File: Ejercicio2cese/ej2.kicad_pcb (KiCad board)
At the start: 4 copper layers, 40.6 x 61 mm, 17 parts, among them J1 DB9-F, J2 CAN, U1 SP3232ECN, U2 AMIS42665TJAA1RG

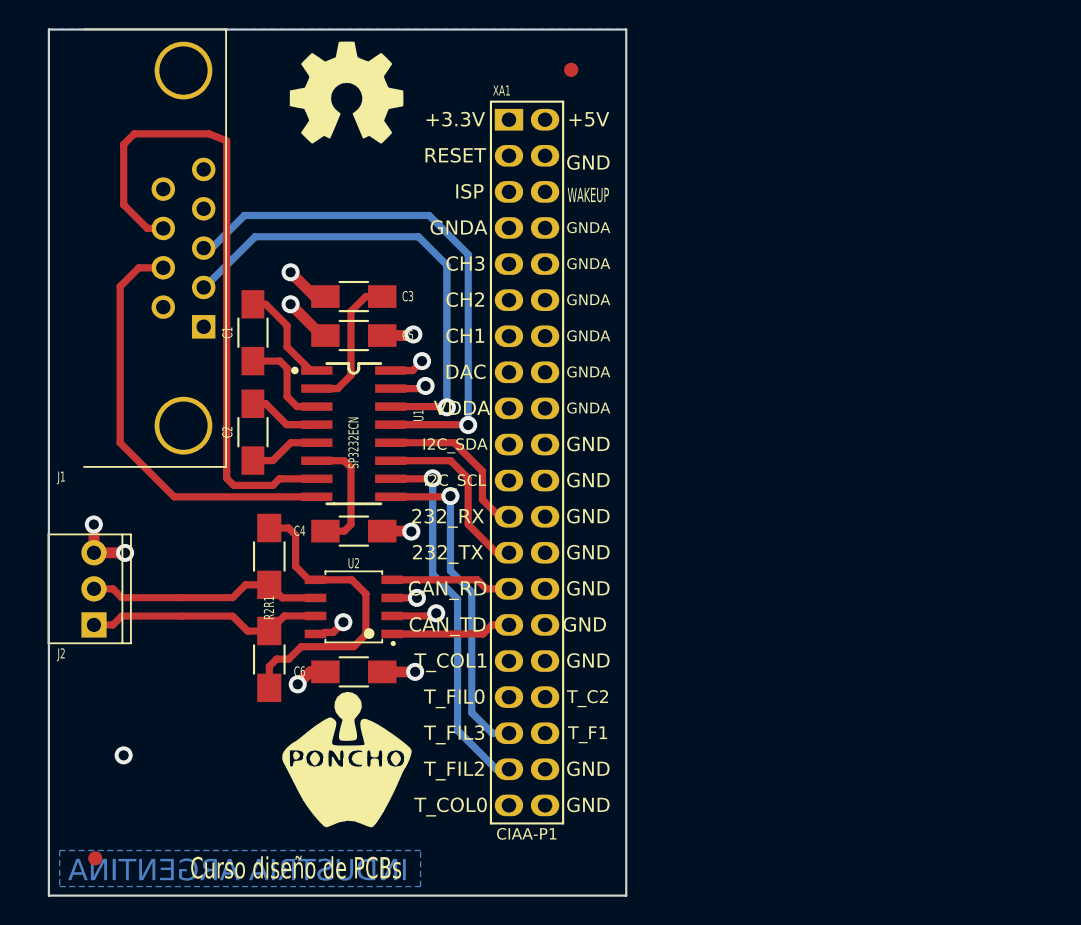
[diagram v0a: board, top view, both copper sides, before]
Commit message: Agrego stackup al Ejercicio2cese.
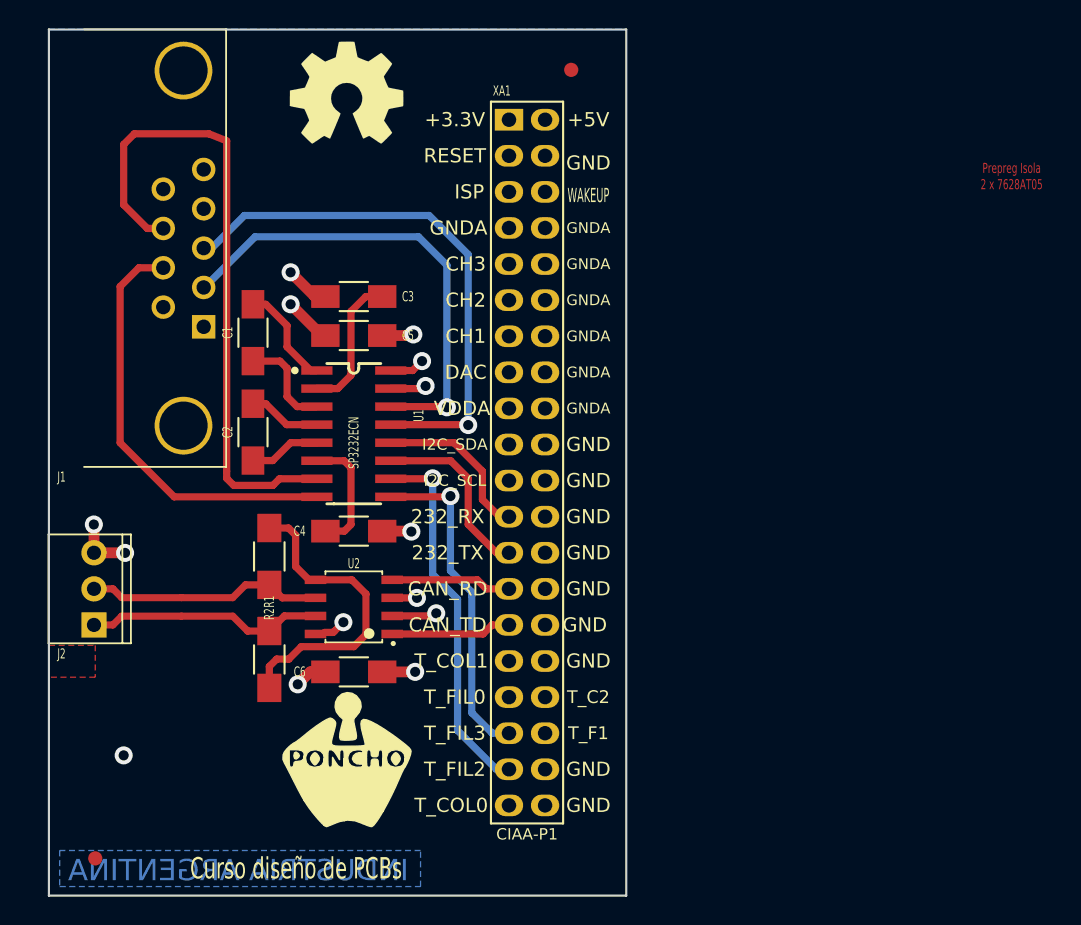
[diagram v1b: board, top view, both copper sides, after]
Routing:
- added copper zone on F.Cu, net (none)
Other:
- board text added: "0,346 mm"
- board text added: "0,760 mm"
- board text added: "1 Oz"
- board text added: "1 Oz = 35 um = 0,035 mm"
- board text added: "L1 - TOP (Signal)"
- board text added: "L2 - GND (Plane)"
- board text added: "L3 - POWER (2 Plane)"
- board text added: "L4 - BOT (Signal)"
- board text added: "Laminate Isola 4 x 7628M"
- board text added: "Prepeg Isola 2 x 7628AT05"
- board text added: "Prepreg Isola 2 x 7628AT05"
- board text removed: "L1 L2"
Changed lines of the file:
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@@
-(kicad_pcb (version 4) (host pcbnew "(2015-09-12 BZR 6188)-product")
+(kicad_pcb (version 4) (host pcbnew 4.0.2+dfsg1-2~bpo8+1-stable)
   (general
     (links 44)
     (no_connects 0)
-    (area 102.159999 73.584999 142.950001 134.695001)
+    (area 80.986905 62.36 236.857859 164.528501)
     (thickness 1.6)
-    (drawings 35)
+    (drawings 52)
     (tracks 169)
     (zones 0)
@@
   (title_block
     (title "Ejercicio 2 - Diseño de PCBs CESE - Poncho RS232 y CAN")
-    (date 2015-11-26)
+    (date 2016-06-03)
     (rev 1.0)
     (company "Instituto Nacional de Tecnología Industrial")
-    (comment 1 "Autores: D.Brengi, D. Alamon y N. Scotti    Licencia:doc/LICENCIA.txt")
+    (comment 1 "Autores: D.Brengi   Licencia:doc/LICENCIA.txt")
   )
   (layers
     (0 TOP signal hide)
     (1 GND power hide)
-    (2 POWER power hide)
-    (31 BOT mixed hide)
+    (2 POWER power)
+    (31 BOT mixed)
     (32 B.Adhes user)
     (33 F.Adhes user hide)
@@
   )
   (setup
-    (last_trace_width 0.508)
+    (last_trace_width 0.3048)
     (user_trace_width 0.3048)
     (user_trace_width 0.4826)
@@
     (user_trace_width 1.27)
     (trace_clearance 0.2794)
-    (zone_clearance 0.3048)
-    (zone_45_only no)
+    (zone_clearance 0.5)
+    (zone_45_only yes)
     (trace_min 0.2794)
     (segment_width 0.127)
@@
       (solder_mask_margin 1.5))
   )
+  (gr_text "1 Oz = 35 um = 0,035 mm" (at 267 109) (layer Dwgs.User)
+    (effects (font (size 1 1) (thickness 0.2)))
+  )
+  (gr_text "0,346 mm" (at 203 97) (layer Dwgs.User)
+    (effects (font (size 1.5 1.5) (thickness 0.2)))
+  )
+  (gr_text "0,760 mm" (at 203 88) (layer Dwgs.User)
+    (effects (font (size 1.5 1.5) (thickness 0.2)))
+  )
+  (gr_text "0,346 mm" (at 203 78) (layer Dwgs.User)
+    (effects (font (size 1.5 1.5) (thickness 0.2)))
+  )
+  (gr_text "1 Oz" (at 199 100) (layer Dwgs.User)
+    (effects (font (size 1 1) (thickness 0.2)))
+  )
+  (gr_text "1 Oz" (at 199 94) (layer Dwgs.User)
+    (effects (font (size 1 1) (thickness 0.2)))
+  )
+  (gr_text "1 Oz" (at 199 81) (layer Dwgs.User)
+    (effects (font (size 1 1) (thickness 0.2)))
+  )
+  (gr_text "1 Oz" (at 199 75) (layer Dwgs.User)
+    (effects (font (size 1 1) (thickness 0.2)))
+  )
+  (gr_text "Laminate Isola\n4 x 7628M" (at 218 87) (layer Dwgs.User)
+    (effects (font (size 1.5 1.5) (thickness 0.2)))
+  )
+  (gr_text "Prepeg Isola\n2 x 7628AT05" (at 218 97) (layer Dwgs.User)
+    (effects (font (size 1.5 1.5) (thickness 0.2)))
+  )
+  (gr_text "Prepeg Isola\n2 x 7628AT05" (at 218 78) (layer Dwgs.User)
+    (effects (font (size 1.5 1.5) (thickness 0.2)))
+  )
+  (gr_text "Prepreg Isola\n2 x 7628AT05" (at 170 84) (layer TOP)
+    (effects (font (size 0.7112 0.4572) (thickness 0.1143)))
+  )
+  (gr_text "L2 - GND (Plane)" (at 242 81) (layer Dwgs.User)
+    (effects (font (size 2 2) (thickness 0.3)))
+  )
+  (gr_text "L4 - BOT (Signal)" (at 229 100) (layer Dwgs.User)
+    (effects (font (size 2 2) (thickness 0.3)) (justify left))
+  )
+  (gr_text "L3 - POWER (2 Plane)" (at 246 94) (layer Dwgs.User)
+    (effects (font (size 2 2) (thickness 0.3)))
+  )
+  (gr_line (start 226.5 100) (end 202 100) (angle 90) (layer Dwgs.User) (width 0.3))
+  (gr_line (start 202 94) (end 226.5 94) (angle 90) (layer Dwgs.User) (width 0.3))
+  (gr_line (start 202.325 81.005) (end 226.455 81.005) (angle 90) (layer Dwgs.User) (width 0.3))
   (gr_text "Colocar \nVerificador\nde layers" (at 87.5 119.9) (layer Dwgs.User)
     (effects (font (size 0.8 0.8) (thickness 0.15)) (justify right))
@@
   (gr_line (start 222.885 164.465) (end 224.79 162.56) (angle 90) (layer Dwgs.User) (width 0.127))
   (gr_line (start 222.885 164.465) (end 220.98 162.56) (angle 90) (layer Dwgs.User) (width 0.127))
-  (gr_text "En un circuito multicapa \nanotar la información del\nstack-up dentro del diseño" (at 170.815 67.31) (layer Dwgs.User)
+  (gr_text "En un circuito multicapa \nanotar la información del\nstack-up dentro del diseño" (at 198 55) (layer Dwgs.User)
     (effects (font (size 2 2) (thickness 0.3) italic) (justify left))
   )
-  (gr_text "L1\n\nL2" (at 203.2 87.63) (layer Dwgs.User)
+  (gr_text "L1 - TOP (Signal)" (at 242 75) (layer Dwgs.User)
     (effects (font (size 2 2) (thickness 0.3)))
   )
-  (gr_line (start 174.625 90.805) (end 198.755 90.805) (angle 90) (layer Dwgs.User) (width 0.3))
-  (gr_line (start 174.625 85.09) (end 198.755 85.09) (angle 90) (layer Dwgs.User) (width 0.3))
-  (gr_text "Terminación superficial: HASL\nEspesor final aprox.: 1,6 mm" (at 191.77 100.965) (layer Dwgs.User)
+  (gr_line (start 202.425 75.005) (end 226.555 75.005) (angle 90) (layer Dwgs.User) (width 0.3))
+  (gr_text "Terminación superficial: HASL\nEspesor final aprox.: 1,6 mm" (at 224 108) (layer Dwgs.User)
     (effects (font (size 2 2) (thickness 0.3)))
   )
-  (gr_text Stack-Up (at 188.595 75.565) (layer Dwgs.User)
+  (gr_text Stack-Up (at 216 64) (layer Dwgs.User)
     (effects (font (size 3 3) (thickness 0.5)))
   )
@@
     )
   )
+  (zone (net 2) (net_name +3.3V) (layer POWER) (hatch edge 0.508)
+    (priority 1)
+    (connect_pads (clearance 0.5))
+    (min_thickness 0.1524)
+    (fill yes (arc_segments 16) (thermal_gap 0.508) (thermal_bridge_width 0.508))
+    (polygon
+      (pts
+        (xy 135.8 74.6) (xy 135.8 110.2) (xy 119.6 110.2) (xy 119.6 107.8) (xy 117.4 105.8)
+        (xy 102.2 105.8) (xy 102.3 74.6)
+      )
+    )
+  )
+  (zone (net 13) (net_name +5V) (layer POWER) (hatch edge 0.508)
+    (connect_pads (clearance 0.2))
+    (min_thickness 0.1524)
+    (fill yes (arc_segments 16) (thermal_gap 0.508) (thermal_bridge_width 0.508))
+    (polygon
+      (pts
+        (xy 141.4 74.6) (xy 102.3 74.6) (xy 102.2 132) (xy 141.4 132)
+      )
+    )
+  )
+  (zone (net 0) (net_name "") (layer TOP) (hatch edge 0.508)
+    (connect_pads (clearance 0))
+    (min_thickness 0.254)
+    (fill yes (arc_segments 16) (thermal_gap 0.508) (thermal_bridge_width 0.762))
+    (polygon
+      (pts
+        (xy 102.25 117) (xy 105.5 117) (xy 105.5 119.25) (xy 102.25 119.25)
+      )
+    )
+  )
   (zone (net 1) (net_name GND) (layer GND) (hatch edge 0.508)
     (connect_pads (clearance 0.2032))
@@
     )
   )
-  (zone (net 2) (net_name +3.3V) (layer POWER) (hatch edge 0.508)
-    (priority 1)
-    (connect_pads (clearance 0.2032))
-    (min_thickness 0.1524)
-    (fill yes (arc_segments 16) (thermal_gap 0.508) (thermal_bridge_width 0.508))
+  (zone (net 0) (net_name "") (layer GND) (hatch edge 0.508)
+    (connect_pads (clearance 0))
+    (min_thickness 0.254)
+    (keepout (tracks allowed) (vias not_allowed) (copperpour not_allowed))
+    (fill (arc_segments 16) (thermal_gap 0.508) (thermal_bridge_width 0.762))
     (polygon
       (pts
-        (xy 135.8 74.6) (xy 135.8 110.2) (xy 119.6 110.2) (xy 119.6 107.8) (xy 117.4 105.8)
-        (xy 103.6 105.8) (xy 103.6 74.6)
+        (xy 102.25 120.75) (xy 105.5 120.75) (xy 105.5 125.75) (xy 102.25 125.75)
       )
     )
   )
-  (zone (net 13) (net_name +5V) (layer POWER) (hatch edge 0.508)
+  (zone (net 0) (net_name "") (layer POWER) (hatch edge 0.508)
     (connect_pads (clearance 0.5))
     (min_thickness 0.1524)
-    (fill yes (arc_segments 16) (thermal_gap 0.508) (thermal_bridge_width 0.508))
+    (keepout (tracks allowed) (vias allowed) (copperpour not_allowed))
+    (fill (arc_segments 16) (thermal_gap 0.508) (thermal_bridge_width 0.508))
     (polygon
       (pts
-        (xy 141.4 74.6) (xy 103.6 74.6) (xy 103.6 132) (xy 141.4 132)
+        (xy 102.25 122.75) (xy 105.5 122.75) (xy 105.5 125.75) (xy 102.25 125.75)
       )
     )

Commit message: Detalles del verificador de capas y limpio bibliotecas del esquemático.
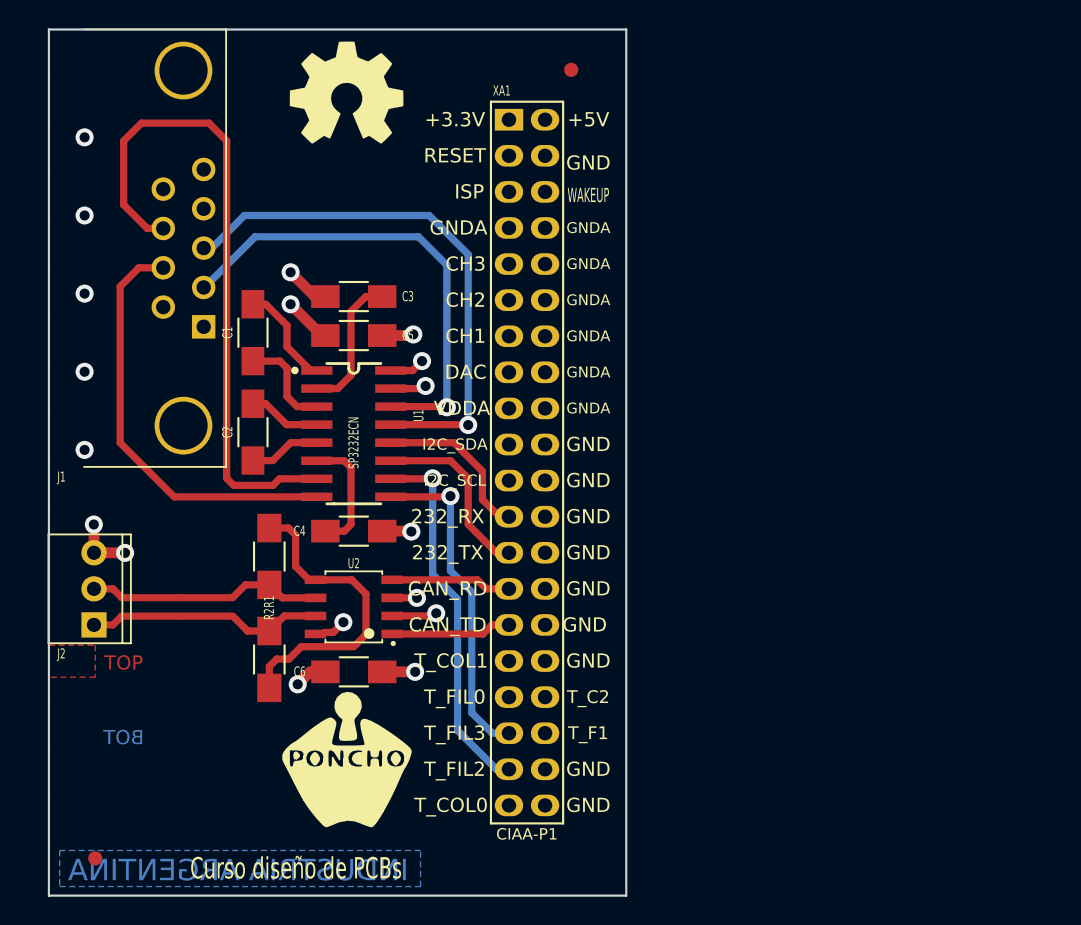
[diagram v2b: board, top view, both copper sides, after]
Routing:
- net GND: track 22.4 -> 52.7 mm, vias 9 -> 14
- net Net-(J1-Pad8): track 45.9 -> 46.8 mm
- net (no net): vias 1 -> 0
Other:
- board text added: "BOT"
- board text added: "GND"
- board text added: "POWER"
- board text added: "TOP"
- board text removed: "Prepreg Isola 2 x 7628AT05"
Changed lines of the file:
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@@
-(kicad_pcb (version 4) (host pcbnew 4.0.2+dfsg1-2~bpo8+1-stable)
+(kicad_pcb (version 4) (host pcbnew "(2015-09-12 BZR 6188)-product")
   (general
     (links 44)
     (no_connects 0)
-    (area 80.986905 62.36 236.857859 164.528501)
+    (area 102.159999 73.584999 142.950001 134.695001)
     (thickness 1.6)
-    (drawings 52)
-    (tracks 169)
+    (drawings 55)
+    (tracks 181)
     (zones 0)
     (modules 17)
@@
   )
   (layers
-    (0 TOP signal hide)
+    (0 TOP signal)
     (1 GND power hide)
-    (2 POWER power)
-    (31 BOT mixed)
+    (2 POWER power hide)
+    (31 BOT signal)
     (32 B.Adhes user)
-    (33 F.Adhes user hide)
+    (33 F.Adhes user)
     (34 B.Paste user)
     (35 F.Paste user)
@@
   )
   (setup
-    (last_trace_width 0.3048)
+    (last_trace_width 0.508)
     (user_trace_width 0.3048)
     (user_trace_width 0.4826)
@@
       (solder_mask_margin 1.5))
   )
+  (gr_text BOT (at 107.5 123.5) (layer BOT)
+    (effects (font (size 1 1) (thickness 0.1)) (justify mirror))
+  )
+  (gr_text POWER (at 108.5 121.75) (layer POWER)
+    (effects (font (size 1 1) (thickness 0.1)))
+  )
+  (gr_text GND (at 107.5 120) (layer GND)
+    (effects (font (size 1 1) (thickness 0.2)))
+  )
+  (gr_text TOP (at 107.5 118.25) (layer TOP)
+    (effects (font (size 1 1) (thickness 0.2)))
+  )
   (gr_text "1 Oz = 35 um = 0,035 mm" (at 267 109) (layer Dwgs.User)
     (effects (font (size 1 1) (thickness 0.2)))
@@
   (gr_text "Prepeg Isola\n2 x 7628AT05" (at 218 78) (layer Dwgs.User)
     (effects (font (size 1.5 1.5) (thickness 0.2)))
-  )
-  (gr_text "Prepreg Isola\n2 x 7628AT05" (at 170 84) (layer TOP)
-    (effects (font (size 0.7112 0.4572) (thickness 0.1143)))
   )
   (gr_text "L2 - GND (Plane)" (at 242 81) (layer Dwgs.User)
@@
   (gr_line (start 97.79 123.825) (end 97.79 133.985) (angle 90) (layer Dwgs.User) (width 0.127))
   (gr_line (start 142.875 134.62) (end 102.235 134.62) (angle 90) (layer Edge.Cuts) (width 0.15))
-  (via (at 107.5 124.75) (size 1.27) (drill 0.7112) (layers TOP BOT) (net 0))
+  (segment (start 104.75 81.25) (end 104.75 86.75) (width 0.508) (layer GND) (net 1))
+  (via (at 104.75 86.75) (size 1.27) (drill 0.7112) (layers TOP BOT) (net 1))
+  (via (at 104.75 92.25) (size 1.27) (drill 0.7112) (layers TOP BOT) (net 1))
+  (segment (start 104.75 97.75) (end 104.75 103.25) (width 0.508) (layer GND) (net 1))
+  (segment (start 104 109.25) (end 104 106.75) (width 0.508) (layer GND) (net 1))
+  (segment (start 104 106.75) (end 104.75 106) (width 0.508) (layer GND) (net 1))
+  (segment (start 104.75 106) (end 104.75 103.25) (width 0.508) (layer GND) (net 1))
+  (via (at 104.75 103.25) (size 1.27) (drill 0.7112) (layers TOP BOT) (net 1))
+  (segment (start 104 109.25) (end 105.24 110.49) (width 0.508) (layer GND) (net 1))
+  (via (at 104.75 97.75) (size 1.27) (drill 0.7112) (layers TOP BOT) (net 1))
+  (segment (start 104.75 97.75) (end 104.75 92.25) (width 0.508) (layer GND) (net 1))
+  (segment (start 104.75 86.75) (end 104.75 92.25) (width 0.508) (layer GND) (net 1))
+  (via (at 104.75 81.25) (size 1.27) (drill 0.7112) (layers TOP BOT) (net 1))
+  (segment (start 105.41 110.49) (end 105.24 110.49) (width 0.508) (layer GND) (net 1))
   (segment (start 122.243304 116.09832) (end 122.328981 116.012644) (width 0.508) (layer TOP) (net 1))
   (segment (start 121.6152 116.09832) (end 122.243304 116.09832) (width 0.508) (layer TOP) (net 1))
@@
   (segment (start 111.053 106.553) (end 107.25 102.75) (width 0.508) (layer TOP) (net 11))
   (segment (start 121.09958 106.553) (end 111.053 106.553) (width 0.508) (layer TOP) (net 11))
-  (segment (start 114.75 104.75) (end 114.75 105.25) (width 0.508) (layer TOP) (net 12))
+  (segment (start 115.25 105.75) (end 114.75 105.25) (width 0.508) (layer TOP) (net 12))
+  (segment (start 115.25 105.75) (end 118 105.75) (width 0.508) (layer TOP) (net 12))
+  (segment (start 110.2876 87.6625) (end 109.1625 87.6625) (width 0.508) (layer TOP) (net 12))
+  (segment (start 107.5 86) (end 109.1625 87.6625) (width 0.508) (layer TOP) (net 12))
+  (segment (start 118.467 105.283) (end 121.09958 105.283) (width 0.508) (layer TOP) (net 12))
   (segment (start 118.467 105.283) (end 118 105.75) (width 0.508) (layer TOP) (net 12))
-  (segment (start 121.09958 105.283) (end 118.467 105.283) (width 0.508) (layer TOP) (net 12))
-  (segment (start 114.75 81.5) (end 113.5 81) (width 0.508) (layer TOP) (net 12))
-  (segment (start 113.5 81) (end 108.25 81) (width 0.508) (layer TOP) (net 12))
-  (segment (start 108.25 81) (end 107.5 81.75) (width 0.508) (layer TOP) (net 12))
-  (segment (start 107.5 81.75) (end 107.5 86) (width 0.508) (layer TOP) (net 12))
-  (segment (start 107.5 86) (end 109.1625 87.6625) (width 0.508) (layer TOP) (net 12))
-  (segment (start 109.1625 87.6625) (end 110.2876 87.6625) (width 0.508) (layer TOP) (net 12))
-  (segment (start 114.75 104.75) (end 114.75 81.5) (width 0.508) (layer TOP) (net 12))
-  (segment (start 115.25 105.75) (end 118 105.75) (width 0.508) (layer TOP) (net 12))
-  (segment (start 114.75 105.25) (end 115.25 105.75) (width 0.508) (layer TOP) (net 12))
+  (segment (start 107.5 81.5) (end 107.5 86) (width 0.508) (layer TOP) (net 12))
+  (segment (start 108.75 80.25) (end 107.5 81.5) (width 0.508) (layer TOP) (net 12))
+  (segment (start 113.5 80.25) (end 108.75 80.25) (width 0.508) (layer TOP) (net 12))
+  (segment (start 114.75 81.5) (end 113.5 80.25) (width 0.508) (layer TOP) (net 12))
+  (segment (start 114.75 105.25) (end 114.75 81.5) (width 0.508) (layer TOP) (net 12))
   (segment (start 125.698 118.872) (end 128.016 118.872) (width 0.762) (layer TOP) (net 13))
   (via (at 128.016 118.872) (size 1.27) (drill 0.7112) (layers TOP BOT) (net 13))
@@
       )
     )
+  )
+  (zone (net 0) (net_name "") (layer BOT) (hatch edge 0.508)
+    (connect_pads (clearance 0.5))
+    (min_thickness 0.254)
+    (keepout (tracks not_allowed) (vias not_allowed) (copperpour not_allowed))
+    (fill (arc_segments 16) (thermal_gap 0.508) (thermal_bridge_width 0.508))
+    (polygon
+      (pts
+        (xy 102.25 124.25) (xy 105.5 124.25) (xy 105.5 125.75) (xy 102.25 125.75)
+      )
+    )
